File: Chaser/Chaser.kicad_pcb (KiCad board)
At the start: 2 copper layers, 48.4 x 50.3 mm, 19 parts, among them U1 NE555P, U2 4017

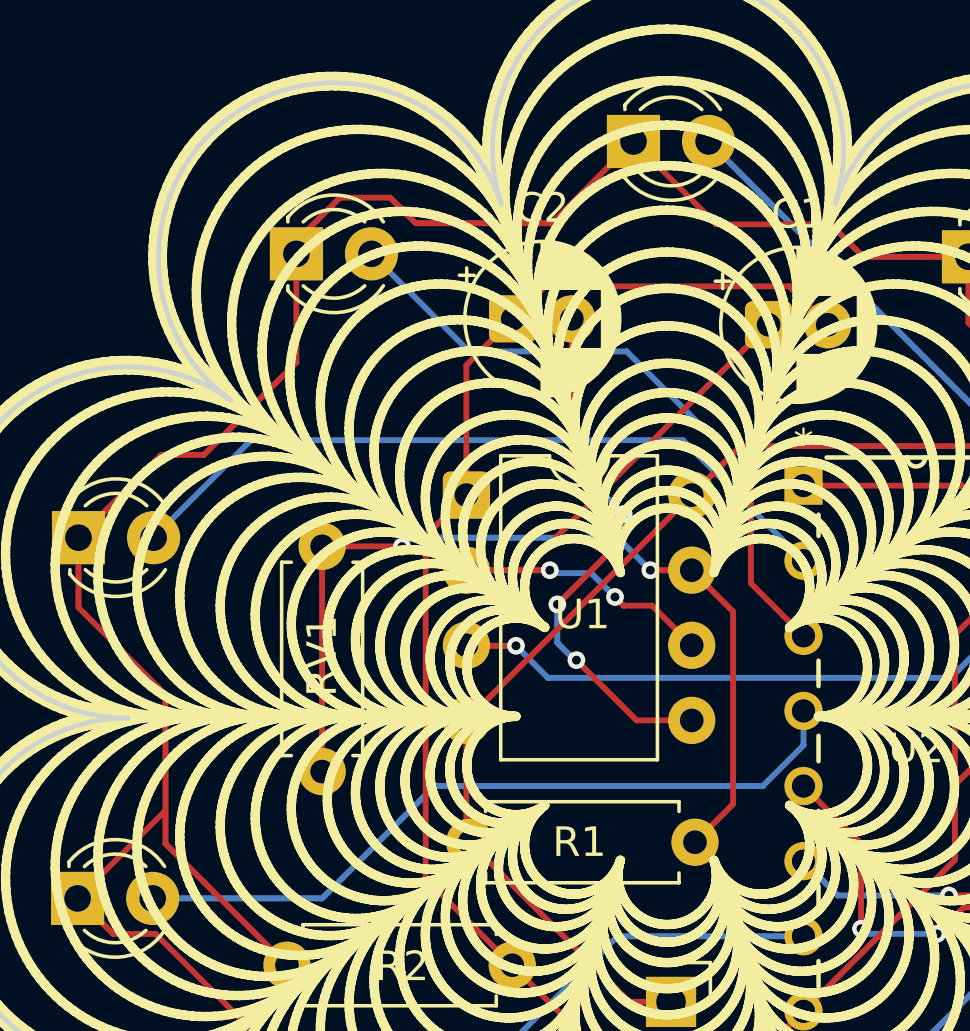
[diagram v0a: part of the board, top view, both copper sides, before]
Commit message: fixed footprints
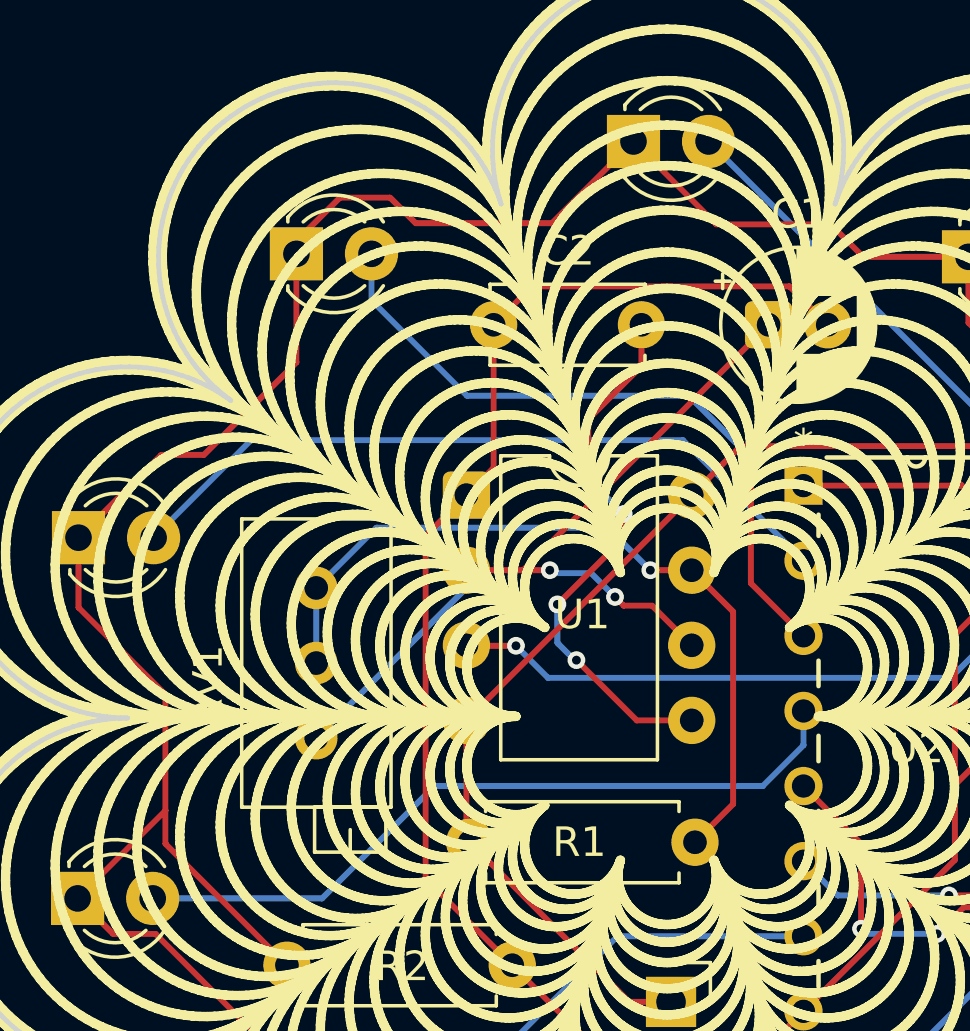
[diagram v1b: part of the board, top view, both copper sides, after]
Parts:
- C2: footprint Capacitor_THT:CP_Radial_D5.0mm_P2.00mm -> Capacitor_THT:C_Disc_D5.0mm_W2.5mm_P5.00mm
- RV1: footprint Resistor_THT:R_Axial_DIN0207_L6.3mm_D2.5mm_P7.62mm_Horizontal -> Potentiometer_THT:Potentiometer_Bourns_3296X_Horizontal
- moved RV1 6.21 mm to (202.2, 48.2)
- moved C2 0.68 mm to (208.2, 39.3)
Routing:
- net TR: track 20.4 -> 28.2 mm
- net Net-(U1-DIS): track 31.0 -> 27.0 mm, vias 2 -> 1
- net Net-(D10-A): track 22.1 -> 23.4 mm
